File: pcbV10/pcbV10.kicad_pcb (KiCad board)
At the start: 2 copper layers, 100 x 100 mm, 215 parts, among them J1 PROG, J10 Fan1, J11 Fan2, J12 VPS, J13 SPK, J14 LoRa Antenna, J15 1B 2A, J16 BME280, J17 CCS811, J18 Power, J19 Supply, J2 Srvo, J20 FAN5V, J21 QWIIC, J22 AudioJack3_SwitchT, J24 AOUT, J3 I2C, J4 1wire, J5 EXT, J6 5V 3V GN 24, J7 485, J8 POWER, J9 GN RGB 5V GN, K1 G6K-2, K2 G6K-2, K3 G6K-2, Q1 BC817, Q2 BC817, Q4 BC817, Q5 IRLML6344, Q6 BC817, Q7 TIP41, Q9 IRLML6344, SW1 BTN BLUE, SW10 5V FAN 24V, SW11 PROG 5V POWER, SW12 RESET, SW2 YELLOW, SW3 GREEN, SW4 RED, SW5 BTN WHITE, SW6 TERM ON, SW7 LED HTR, SW8 REL ROT, SW9 SNS MOV, U1 AMS1117, U10 LM358, U11 FUSB302BMPX, U12 BME680, U13 BME280, U14 IPS_240_240, U15 CCS811, U16 MODULE_STEPDOWN, U17 RFM95W-868S2, U18 MD8002A, U19 DS18B20, U2 ESP32-WROOM-32, U20 BH1750, U21 BTS462T, U22 AM612, U23 MPU-6050, U24 SRV05, U3 ICS-43432, U4 CH340C, U5 UDA1334, U6 MAX3485, U7 DS18B20, U8 HDC1080, U9 EUP3458, X1 FAN_6024, X2 XGZP6897D

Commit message: Various
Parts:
- removed C59: u1, Capacitor_SMD:C_0603_1608Metric
- removed D16: SS34, Diode_SMD:D_SMA
- removed R29: M1, Resistor_SMD:R_0603_1608Metric
- removed U8: HDC1080, Package_SON:Texas_PWSON-N6
- added C21: 1u, Capacitor_SMD:C_0805_2012Metric_Pad1.18x1.45mm_HandSolder, B.Cu at (83.9, 110.2)
- added C34: 100u, Capacitor_SMD:C_1206_3216Metric_Pad1.33x1.80mm_HandSolder, B.Cu at (80.0, 110.8)
- added C37: u1, Capacitor_SMD:C_0603_1608Metric, F.Cu at (89.0, 101.0)
- added C60: 10u, Capacitor_SMD:C_1206_3216Metric, F.Cu at (68.8, 105.6)
- added C61: 10u, Capacitor_SMD:C_0603_1608Metric, F.Cu at (71.2, 138.0)
- added FB1: 100R, Inductor_SMD:L_0805_2012Metric, F.Cu at (79.8, 111.3)
- added JP5: 5V AMP 3V, Jumper:SolderJumper-3_P1.3mm_Open_RoundedPad1.0x1.5mm_NumberLabels, F.Cu at (80.2, 114.3)
- added NT1: 1, NetTie:NetTie-2_SMD_Pad0.5mm, B.Cu at (128.4, 99.9)
- added NT2: 1, NetTie:NetTie-2_SMD_Pad0.5mm, F.Cu at (121.5, 101.0)
- added U25: NS4168, liebler_SEMICONDUCTORS:SOIC-8_3.9x4.9mm_Pitch1.27mm_pad_handsolder, B.Cu at (89.7, 108.0)
- added U26: MSM261D4030H1CPM, liebler_SEMICONDUCTORS:MSM261D4030H1CPM, F.Cu at (91.8, 100.3)
- C35: value 10n -> u1
- C39: value u1 -> 10u
- J12: footprint Connector_PinHeader_2.54mm:PinHeader_2x25_P2.54mm_Vertical -> Connector_PinHeader_2.54mm:PinHeader_2x29_P2.54mm_Vertical
- J19: value Supply -> SPK; footprint Connector_PinHeader_2.54mm:PinHeader_2x04_P2.54mm_Vertical -> Connector_Wire:SolderWire-0.1sqmm_1x02_P3.6mm_D0.4mm_OD1mm
- L2: value 6u8 -> 4u7
- SW6: value TERM ON -> OFF TERM ON
- U3: value ICS-43432 -> AHT21; footprint liebler_SEMICONDUCTORS:MIC_ICS-43432 -> liebler_SEMICONDUCTORS:AHT21
- U9: value EUP3458 -> RY8310
- moved J19 73.6 mm to (82.0, 108.2), turned to -90 degrees
- moved U3 34.7 mm to (74.7, 137.8), turned to 0 degrees
- moved J12 10.2 mm to (142.5, 67.1)
- moved R46 8.14 mm to (77.8, 104.8)
- moved C39 6.40 mm to (87.5, 101.0)
- moved C55 6.20 mm to (125.5, 60.2), turned to -90 degrees
- moved C35 4.85 mm to (73.5, 107.4), turned to 180 degrees
- moved C11 4.31 mm to (89.3, 104.3)
- moved C13 4.31 mm to (90.8, 104.3)
- moved R45 3.95 mm to (76.2, 104.8), turned to 90 degrees
- moved C54 3.95 mm to (116.4, 60.1), turned to -90 degrees
- moved R40 3.27 mm to (87.8, 104.3), turned to 90 degrees
- moved R52 3.20 mm to (118.8, 71.8)
- moved R51 3.18 mm to (118.8, 70.2)
- moved C33 3.05 mm to (70.7, 105.0)
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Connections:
- net Net-(J13-Pad1) renamed /analog_amp/SPK+
- net Net-(J13-Pad2) renamed /analog_amp/SPK-
- C23 pad 2: GND -> GNDA
- C25 pad 1: +5V -> +5VA
- C25 pad 2: GND -> GNDA
- C26 pad 1: +5V -> +5VA
- C26 pad 2: GND -> GNDA
- J12 pad 1: K1_A1 -> +3V3
- J12 pad 10: K1_21 -> K1_A1
- J12 pad 11: K1_22 -> K1_11
- J12 pad 12: K1_22 -> K1_11
- J12 pad 13: K1_24 -> K1_12
- J12 pad 14: K1_24 -> K1_12
- J12 pad 15: K2_A1 -> K1_14
- J12 pad 16: K2_A1 -> K1_14
- J12 pad 17: K2_11 -> K1_21
- J12 pad 18: K2_11 -> K1_21
- J12 pad 19: K2_12 -> K1_22
- J12 pad 2: K1_A1 -> +3V3
- J12 pad 20: K2_12 -> K1_22
- J12 pad 21: K2_14 -> K1_24
- J12 pad 22: K2_14 -> K1_24
- J12 pad 23: K2_21 -> K2_A1
- J12 pad 24: K2_21 -> K2_A1
- J12 pad 25: K2_22 -> K2_11
- J12 pad 26: K2_22 -> K2_11
- J12 pad 27: K2_24 -> K2_12
- J12 pad 28: K2_24 -> K2_12
- J12 pad 29: Net-(J12-Pad29) -> K2_14
- J12 pad 3: K1_11 -> GND
- J12 pad 30: Net-(J12-Pad29) -> K2_14
- J12 pad 31: K3_11 -> K2_21
- J12 pad 32: K3_11 -> K2_21
- J12 pad 33: K3_12 -> K2_22
- J12 pad 34: K3_12 -> K2_22
- J12 pad 35: K3_14 -> K2_24
- J12 pad 36: K3_14 -> K2_24
- J12 pad 37: K3_21 -> Net-(J12-Pad37)
- J12 pad 38: K3_21 -> Net-(J12-Pad37)
- J12 pad 39: K3_22 -> K3_11
- J12 pad 4: K1_11 -> GND
- J12 pad 40: K3_22 -> K3_11
- J12 pad 41: K3_24 -> K3_12
- J12 pad 42: K3_24 -> K3_12
- J12 pad 43: SW_BLUE -> K3_14
- J12 pad 44: SW_BLUE -> K3_14
- J12 pad 45: SW_WHITE -> K3_21
- J12 pad 46: SW_WHITE -> K3_21
- J12 pad 47: LED_BLUE -> K3_22
- J12 pad 48: LED_BLUE -> K3_22
- J12 pad 49: LED_WHITE -> K3_24
- J12 pad 5: K1_12 -> +5V
- J12 pad 50: LED_WHITE -> K3_24
- J12 pad 6: K1_12 -> +5V
- J12 pad 7: K1_14 -> +5V
- J12 pad 8: K1_14 -> +5V
- J12 pad 9: K1_21 -> K1_A1
- J19 pad 1: +3V3 -> /analog_amp/VoP
- J19 pad 2: +3V3 -> /analog_amp/VoN
- R37 pad 2: Net-(J12-Pad29) -> Net-(J12-Pad37)
- U18 pad 1: GND -> GNDA
- U18 pad 6: +5V -> +5VA
- U18 pad 7: GND -> GNDA
- U3 pad 1: GND -> unconnected-(U3-Pad1)
- U3 pad 2: GND -> +3V3
- U3 pad 3: +3V3 -> SCL
- U3 pad 4: GND -> SDA
- U3 pad 5: I2S_WS -> GND
- U3 pad 6: I2S_SCK -> unconnected-(U3-Pad6)
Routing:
- net Net-(J12-Pad29): track 52.7 -> 0.00 mm, vias 1 -> 0
- net Net-(J12-Pad37): track 0.00 -> 52.2 mm, vias 0 -> 1
- net GNDA: track 0.00 -> 19.8 mm
- net I2S_SD: track 16.5 -> 30.0 mm
- net SCL: track 219.7 -> 210.1 mm, vias 8 -> 7
- net /analog_amp/VoP: track 0.00 -> 8.91 mm
- net Net-(R45-Pad2): track 11.9 -> 3.19 mm
- net GND: track 163.7 -> 155.8 mm, vias 228 -> 231
- net Net-(C21-Pad1): track 0.00 -> 7.33 mm, vias 0 -> 1
- net SDA: track 228.4 -> 221.5 mm, vias 6 -> 5
- net /psu/SW: track 10.4 -> 4.19 mm
- net /psu/5Vx: track 36.8 -> 42.2 mm, vias 1 -> 3
- net /analog_amp/VoN: track 0.00 -> 5.24 mm
- net I2S_SCK: track 28.1 -> 33.3 mm, vias 0 -> 3
- net +3V3: track 548.3 -> 553.4 mm, vias 10 -> 29
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- added copper zone on B.Cu, net +3V3
- added copper zone on F.Cu, net +3V3
- added copper zone on F.Cu, net GNDA
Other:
- board text added: "2022-05-30 Klaus Liebler"
- board text added: "3V GN SC SD GN NC NC NC"
- board text added: "Alle Jumper in der Mini-Ausführung statt lötbare Module lieber diesen miniPCIE-Connector Modbus nicht mehr über RJ11 Verstärker NS4168, aber Problem: Lautstärke nur mit Software!"
- board text added: "lab@home 12"
- board text removed: "2022-03-29 Klaus Liebler"
- board text removed: "Alle Jumper in der Mini-Ausführung statt lötbare Module lieber diesen miniPCIE-Connector Die 5V/3V/GND direkt mit dem Relais_Connector koppeln Modbus nicht mehr über RJ11"
- board text removed: "Micro"
- board text removed: "Testen mit ES8374"
- board text removed: "lab@home 11"

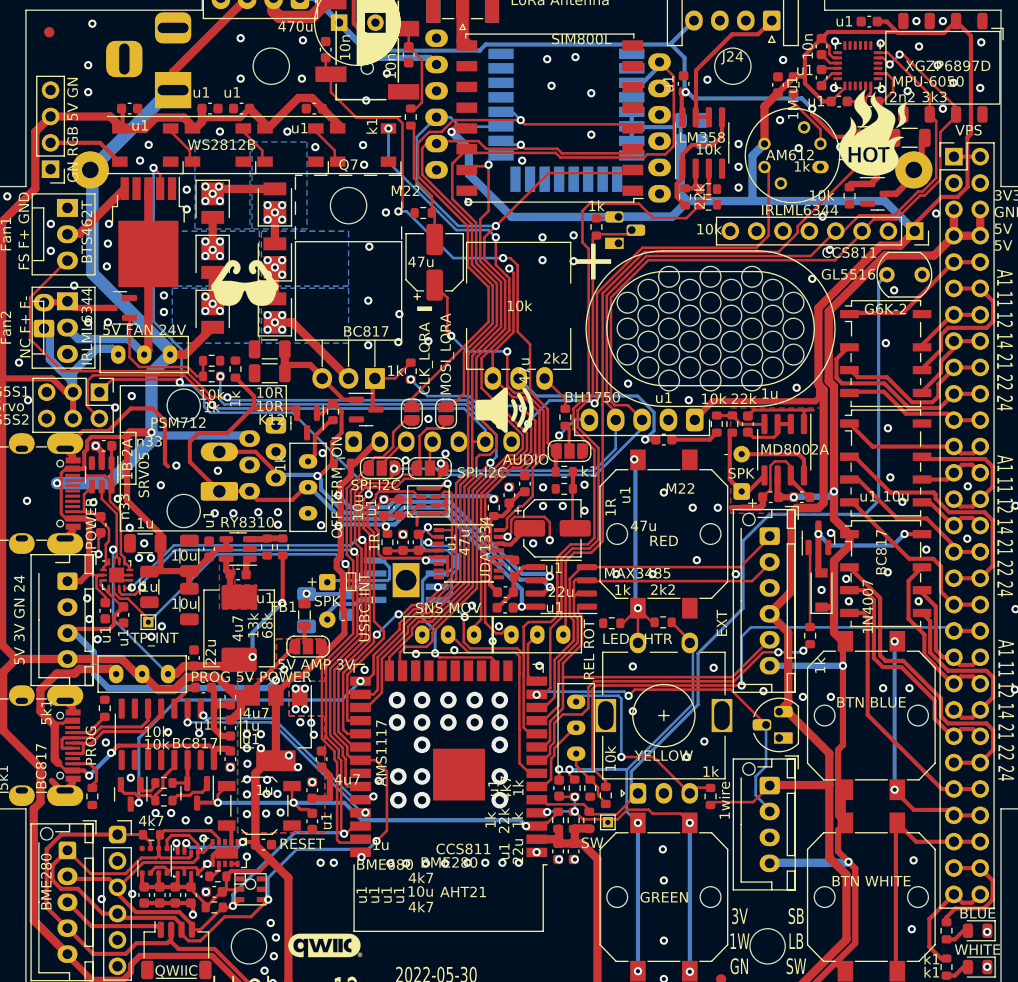
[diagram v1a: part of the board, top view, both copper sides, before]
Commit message: Bugfix: digital amplifier not in standby
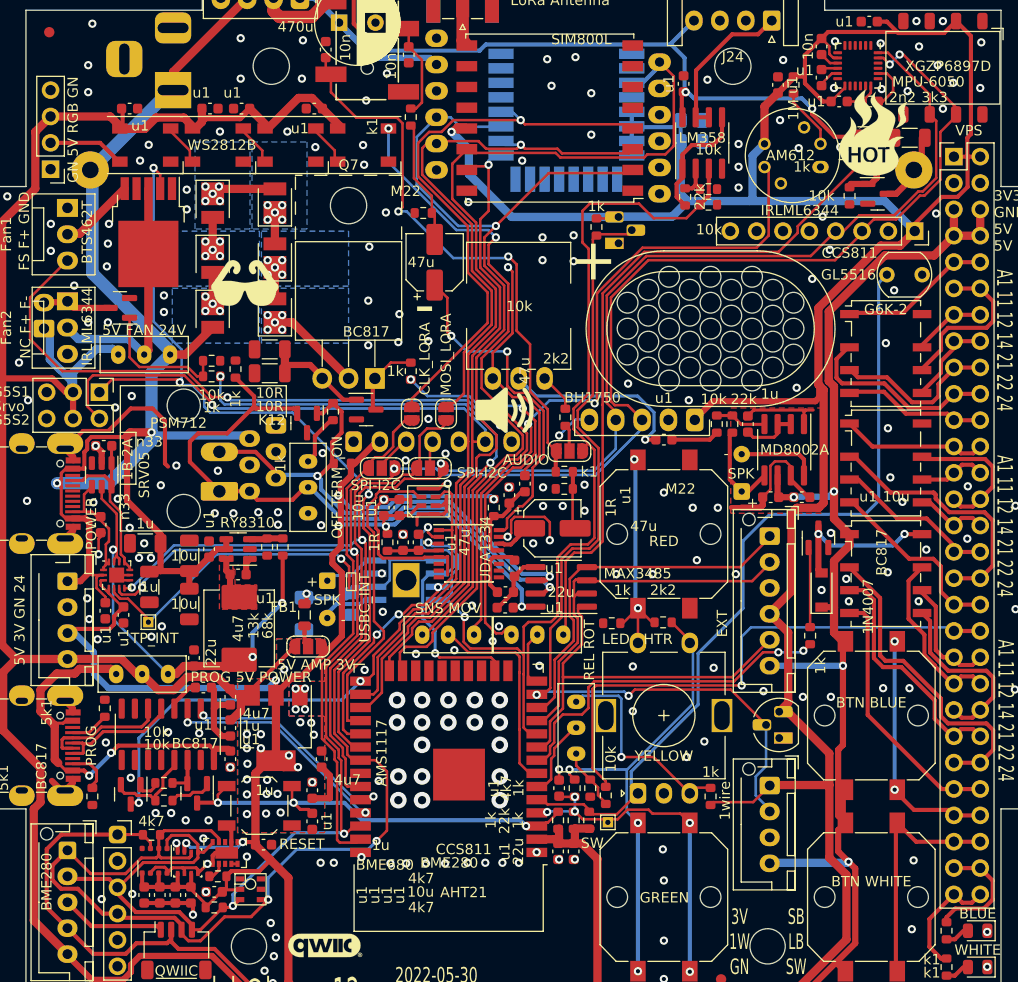
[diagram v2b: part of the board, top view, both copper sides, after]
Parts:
- J9: value GN RGB 5V GN -> GN 5V RGB GN
- moved C21 0.50 mm to (84.4, 110.2)
- moved C34 0.43 mm to (79.8, 111.2)
- moved J19 0.15 mm to (82.0, 108.0)
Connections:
- U25 pad 1: GND -> Net-(C21-Pad1)
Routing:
- net Net-(C21-Pad1): track 7.33 -> 15.4 mm
- net /analog_amp/VoP: track 8.91 -> 4.67 mm
- net I2S_WS: track 26.3 -> 24.7 mm
- net /psu/5Vx: track 42.2 -> 40.7 mm
- net /psu/SW: track 4.19 -> 2.95 mm
- net GND: track 155.8 -> 154.7 mm, vias 231 -> 232
- net SDA: track 221.5 -> 220.6 mm
- net AUDIO: track 96.8 -> 96.0 mm
- net +5V: track 376.1 -> 375.5 mm
- net +24V: track 212.5 -> 211.9 mm
